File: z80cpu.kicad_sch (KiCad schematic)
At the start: 6 parts

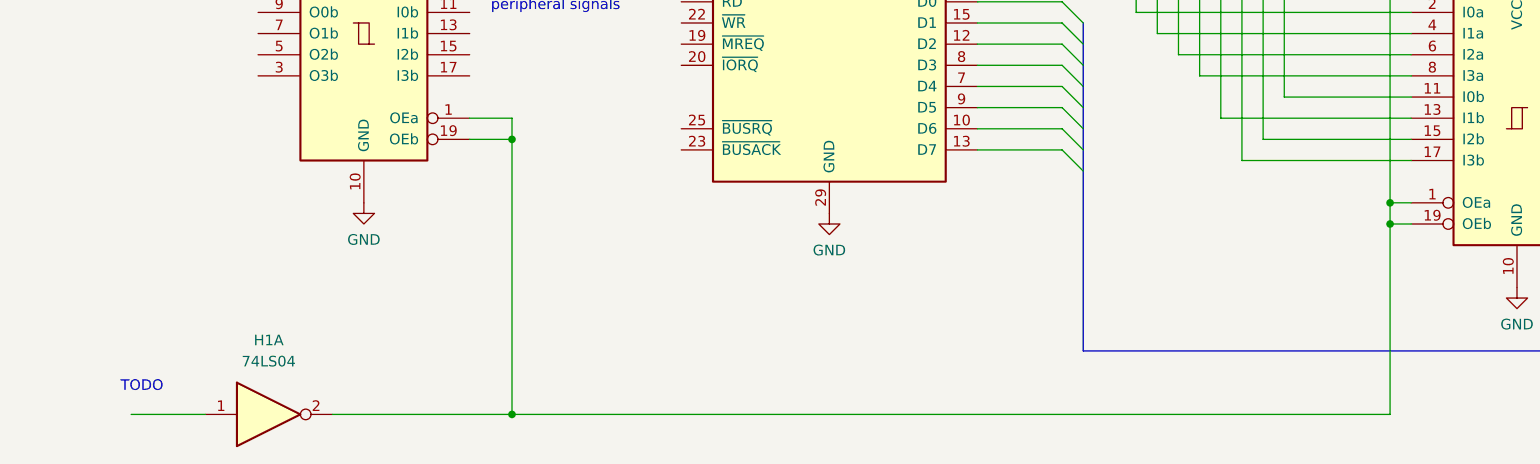
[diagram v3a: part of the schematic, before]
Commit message: Fixed addr order in mem mux, busack on z80 buffers
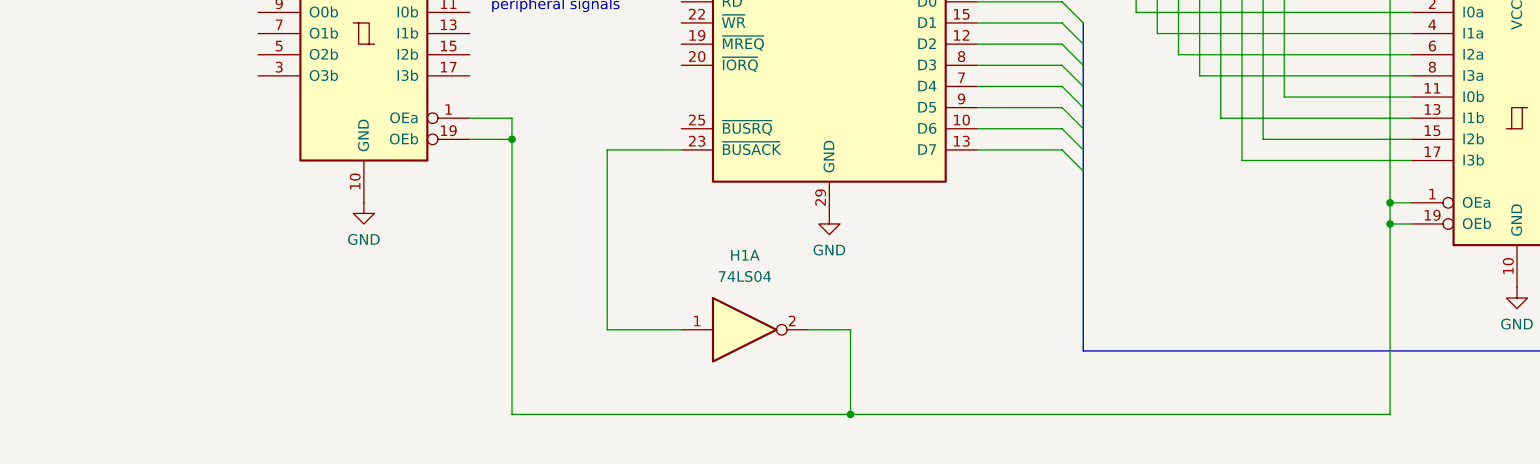
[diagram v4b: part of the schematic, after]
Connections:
- net at H1.1: now also F2-F5.23 (~{BUSACK})
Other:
- note removed: "TODO"
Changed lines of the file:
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@@
   (junction (at 182.88 54.61) (diameter 0) (color 0 0 0 0)
   )
+  (junction (at 118.11 134.62) (diameter 0) (color 0 0 0 0)
+  )
   (junction (at 182.88 111.76) (diameter 0) (color 0 0 0 0)
   )
   (junction (at 77.47 101.6) (diameter 0) (color 0 0 0 0)
   )
-  (junction (at 77.47 134.62) (diameter 0) (color 0 0 0 0)
-  )
   (junction (at 182.88 109.22) (diameter 0) (color 0 0 0 0)
   )
@@
     (stroke (width 0) (type default))
   )
-  (wire (pts (xy 31.75 134.62) (xy 40.64 134.62))
-    (stroke (width 0) (type default))
-  )
   (wire (pts (xy 170.18 46.99) (xy 170.18 57.15))
     (stroke (width 0) (type default))
@@
     (stroke (width 0) (type default))
   )
+  (wire (pts (xy 97.79 102.87) (xy 88.9 102.87))
+    (stroke (width 0) (type default))
+  )
   (wire (pts (xy 160.02 72.39) (xy 160.02 93.98))
     (stroke (width 0) (type default))
@@
     (stroke (width 0) (type default))
   )
+  (wire (pts (xy 88.9 102.87) (xy 88.9 124.46))
+    (stroke (width 0) (type default))
+  )
   (wire (pts (xy 133.35 85.09) (xy 143.51 85.09))
     (stroke (width 0) (type default))
@@
     (stroke (width 0) (type default))
   )
+  (wire (pts (xy 88.9 124.46) (xy 97.79 124.46))
+    (stroke (width 0) (type default))
+  )
   (wire (pts (xy 152.4 86.36) (xy 185.42 86.36))
     (stroke (width 0) (type default))
@@
     (stroke (width 0) (type default))
   )
+  (wire (pts (xy 118.11 134.62) (xy 182.88 134.62))
+    (stroke (width 0) (type default))
+  )
   (wire (pts (xy 133.35 52.07) (xy 165.1 52.07))
     (stroke (width 0) (type default))
@@
     (stroke (width 0) (type default))
   )
-  (wire (pts (xy 77.47 134.62) (xy 182.88 134.62))
+  (wire (pts (xy 77.47 134.62) (xy 118.11 134.62))
     (stroke (width 0) (type default))
   )
@@
     (stroke (width 0) (type default))
   )
+  (wire (pts (xy 118.11 124.46) (xy 118.11 134.62))
+    (stroke (width 0) (type default))
+  )
   (wire (pts (xy 133.35 95.25) (xy 143.51 95.25))
     (stroke (width 0) (type default))
@@
     (stroke (width 0) (type default))
   )
-  (wire (pts (xy 55.88 134.62) (xy 77.47 134.62))
-    (stroke (width 0) (type default))
-  )
   (wire (pts (xy 157.48 91.44) (xy 185.42 91.44))
     (stroke (width 0) (type default))
@@
     (stroke (width 0) (type default))
   )
+  (wire (pts (xy 113.03 124.46) (xy 118.11 124.46))
+    (stroke (width 0) (type default))
+  )
   (wire (pts (xy 210.82 41.91) (xy 220.98 41.91))
     (stroke (width 0) (type default))
@@
   (bus (pts (xy 223.52 101.6) (xy 223.52 104.14))
     (stroke (width 0) (type default))
-  )
-  (text "TODO" (at 30.48 132.08 0)
-    (effects (font (size 1.27 1.27)) (justify left bottom))
   )
   (text "TODO\n<-- Z80 to ---\nperipheral signals" (at 74.93 86.36 0)
@@
         (path "/12a6dbe3-008d-4c5b-88f6-9f1c816060be/1847fdc4-53d8-4940-8c5f-7a326599bae2"
           (reference "U?") (unit 1)
-        )
-      )
-    )
-  )
-  (symbol (lib_id "74xx:74LS04") (at 48.26 134.62 0) (unit 1)
-    (in_bom yes) (on_board yes) (dnp no) (fields_autoplaced)
-    (property "Reference" "H1" (at 48.26 125.73 0)
-      (effects (font (size 1.27 1.27)))
-    )
-    (property "Value" "74LS04" (at 48.26 128.27 0)
-      (effects (font (size 1.27 1.27)))
-    )
-    (property "Footprint" "" (at 48.26 134.62 0)
-      (effects (font (size 1.27 1.27)) hide)
-    )
-    (property "Datasheet" "http://www.ti.com/lit/gpn/sn74LS04" (at 48.26 134.62 0)
-      (effects (font (size 1.27 1.27)) hide)
-    )
-    (pin "1")
-    (pin "2")
-    (pin "3")
-    (pin "4")
-    (pin "5")
-    (pin "6")
-    (pin "8")
-    (pin "9")
-    (pin "10")
-    (pin "11")
-    (pin "12")
-    (pin "13")
-    (pin "14")
-    (pin "7")
-    (instances
-      (project "ceda"
-        (path "/12a6dbe3-008d-4c5b-88f6-9f1c816060be/1847fdc4-53d8-4940-8c5f-7a326599bae2"
-          (reference "H1") (unit 1)
         )
       )
@@
         )
       )
+    )
+  )
+  (symbol (lib_id "74xx:74LS04") (at 105.41 124.46 0) (unit 1)
+    (in_bom yes) (on_board yes) (dnp no) (fields_autoplaced)
+    (property "Reference" "H1" (at 105.41 115.57 0)
+      (effects (font (size 1.27 1.27)))
+    )
+    (property "Value" "74LS04" (at 105.41 118.11 0)
+      (effects (font (size 1.27 1.27)))
+    )
+    (property "Footprint" "" (at 105.41 124.46 0)
+      (effects (font (size 1.27 1.27)) hide)
+    )
+    (property "Datasheet" "http://www.ti.com/lit/gpn/sn74LS04" (at 105.41 124.46 0)
+      (effects (font (size 1.27 1.27)) hide)
+    )
+    (pin "1")
+    (pin "2")
+    (pin "3")
+    (pin "4")
+    (pin "5")
+    (pin "6")
+    (pin "8")
+    (pin "9")
+    (pin "10")
+    (pin "11")
+    (pin "12")
+    (pin "13")
+    (pin "14")
+    (pin "7")
+    (instances
+      (project "ceda"
+        (path "/12a6dbe3-008d-4c5b-88f6-9f1c816060be/1847fdc4-53d8-4940-8c5f-7a326599bae2"
+          (reference "H1") (unit 1)
+        )
+      )

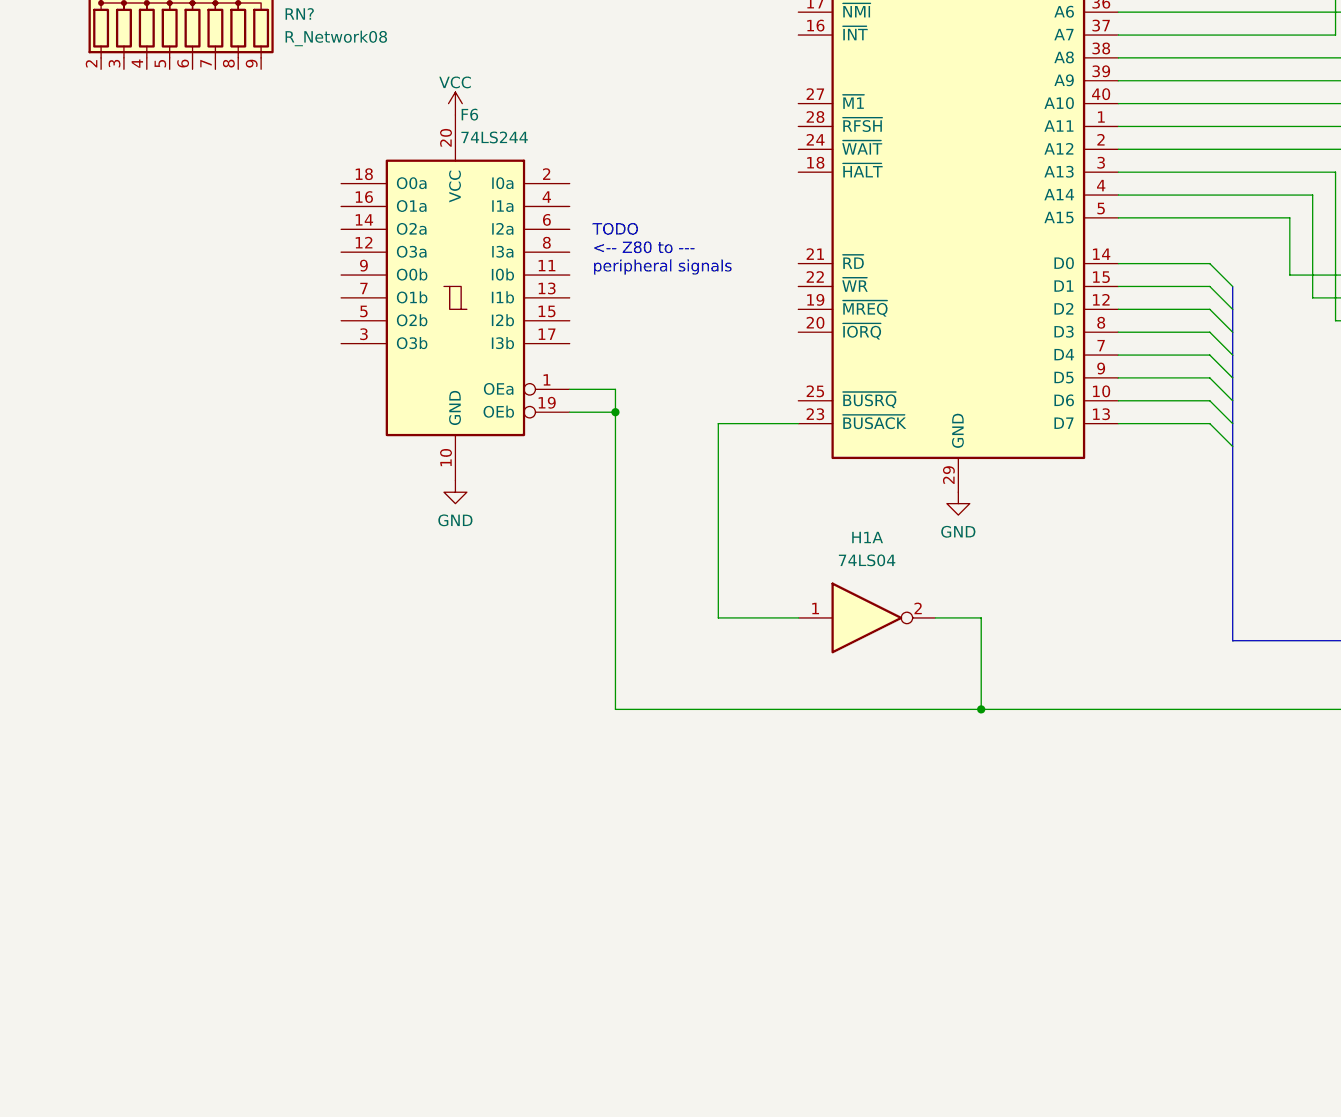
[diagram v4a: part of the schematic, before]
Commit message: Found both ROM CE and OE
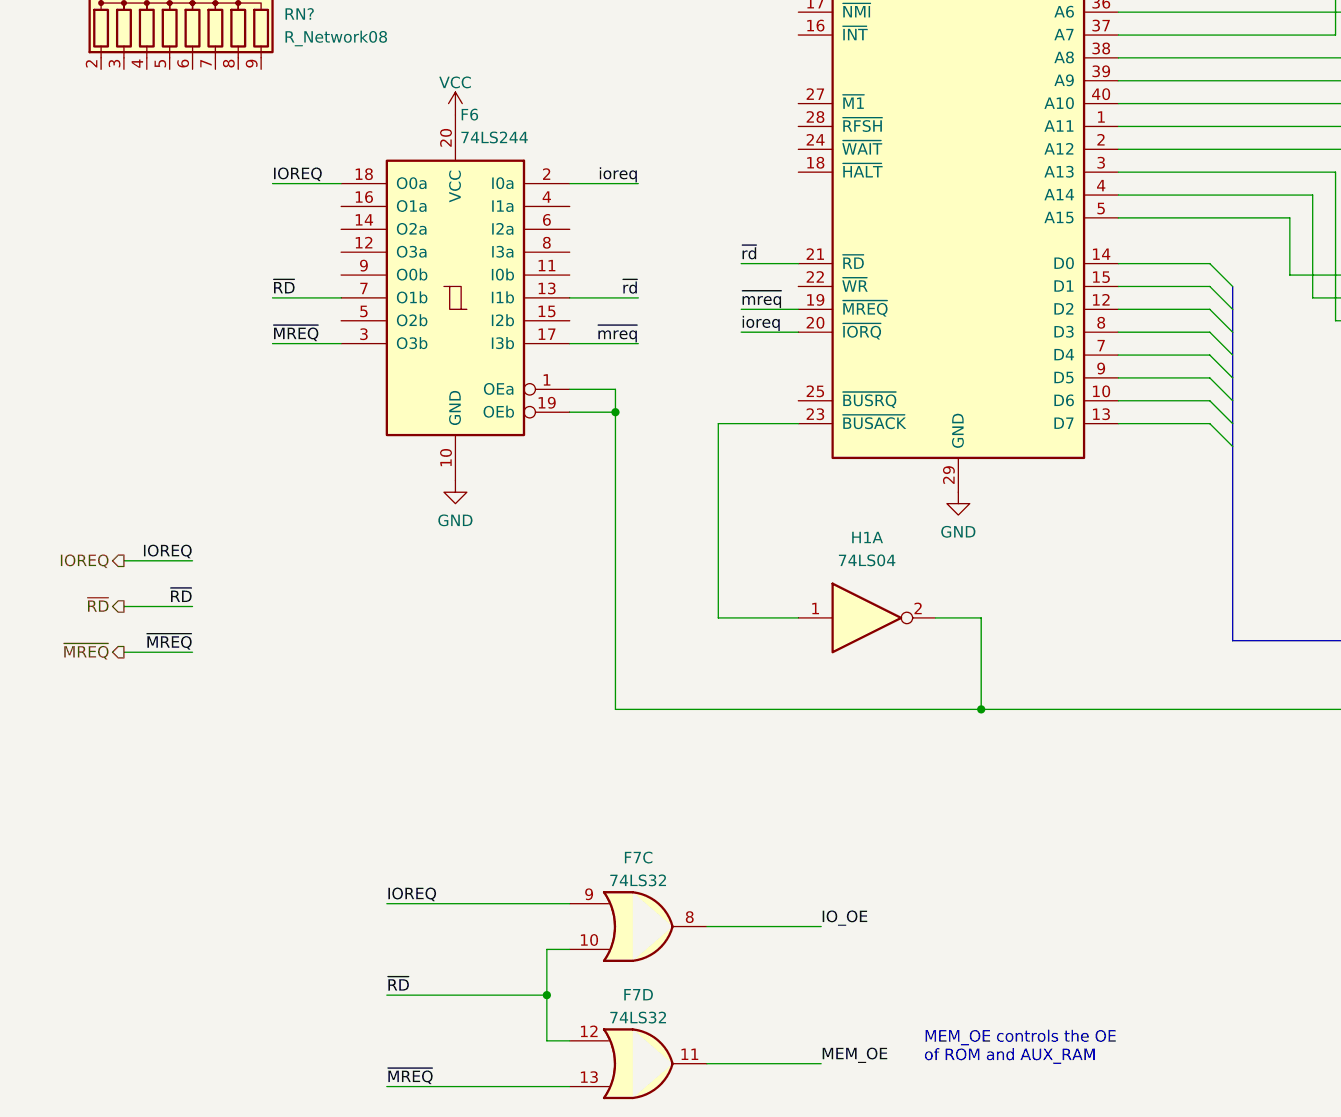
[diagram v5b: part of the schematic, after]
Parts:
- added F7: 74LS32, symbol 74xx:74LS32
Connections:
- net ~{mreq}: now reaches F2-F5.19 (~{MREQ})
- net ~{mreq}: now also F6.17 (I3b)
- net ioreq: now reaches F2-F5.20 (~{IORQ})
- net ioreq: now also F6.2 (I0a)
- net ~{rd}: now reaches F2-F5.21 (~{RD})
- net ~{rd}: now also F6.13 (I1b)
- net IOREQ: now reaches F6.18 (O0a)
- net IOREQ: now also F7.9
- net ~{MREQ}: now reaches F6.3 (O3b)
- net ~{MREQ}: now also F7.13
- net ~{RD}: now reaches F6.7 (O1b)
- net ~{RD}: now also F7.10, F7.12
- new net IO_OE: F7.8
- new net MEM_OE: F7.11
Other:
- note added: "MEM_OE controls the OE of ROM and AUX_RAM"
- note removed: "TODO <-- Z80 to --- peripheral signals"

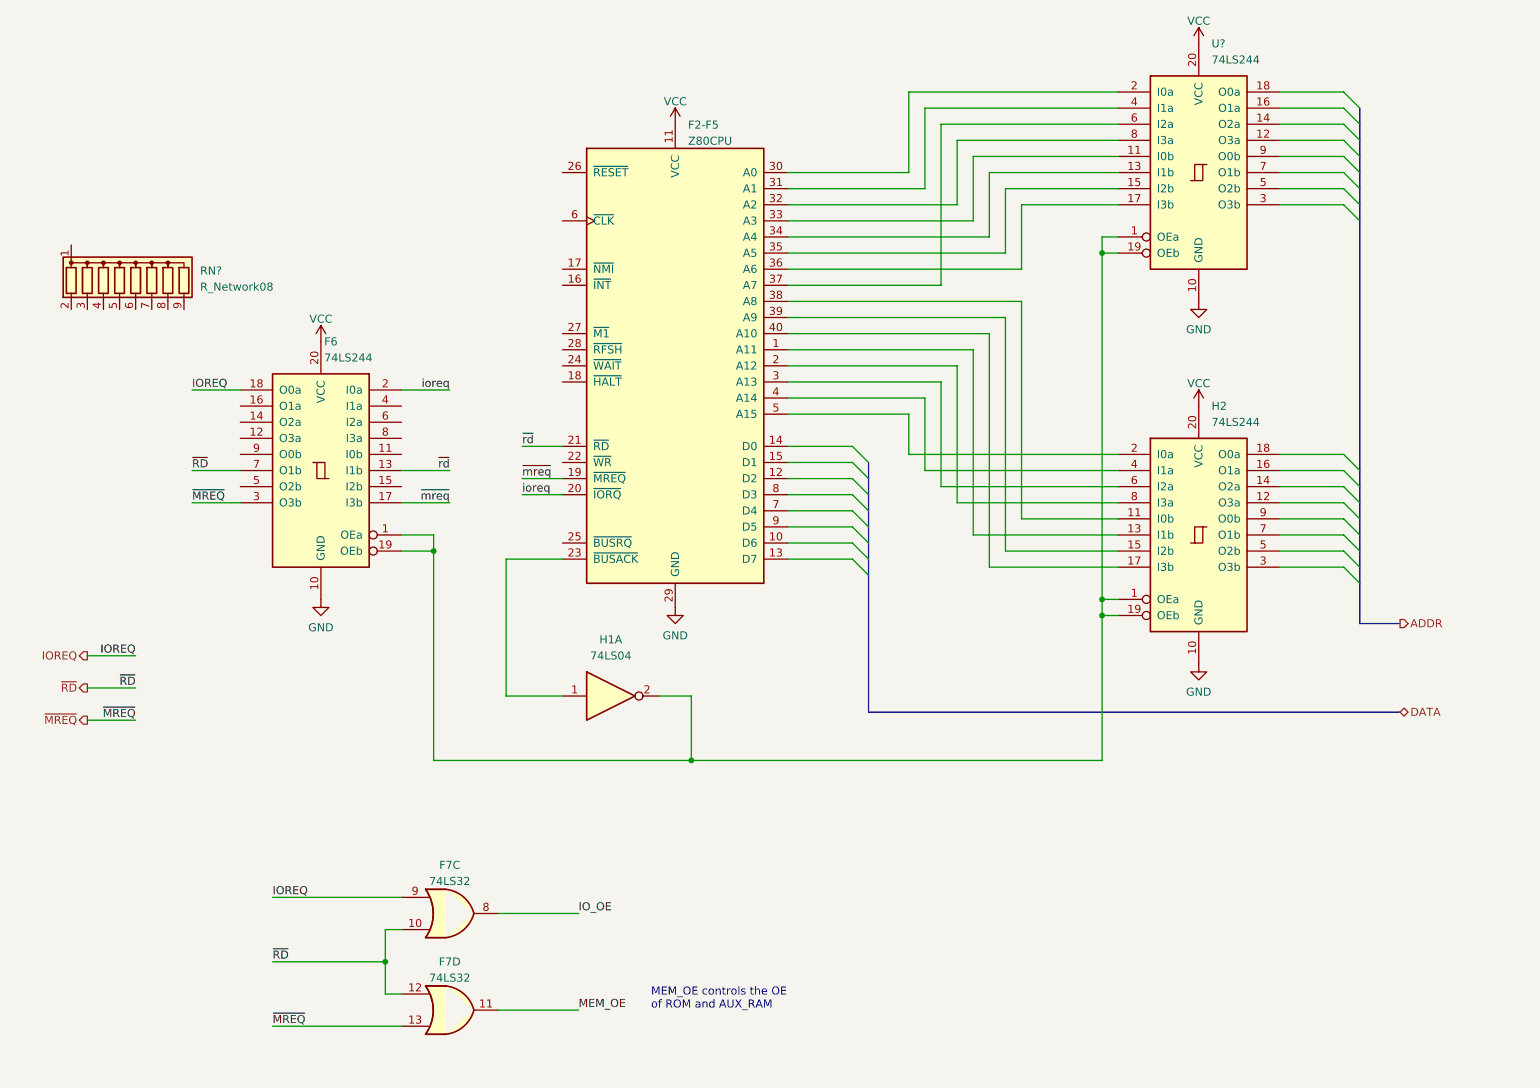
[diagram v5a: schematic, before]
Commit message: Found WR signal and fixed RD
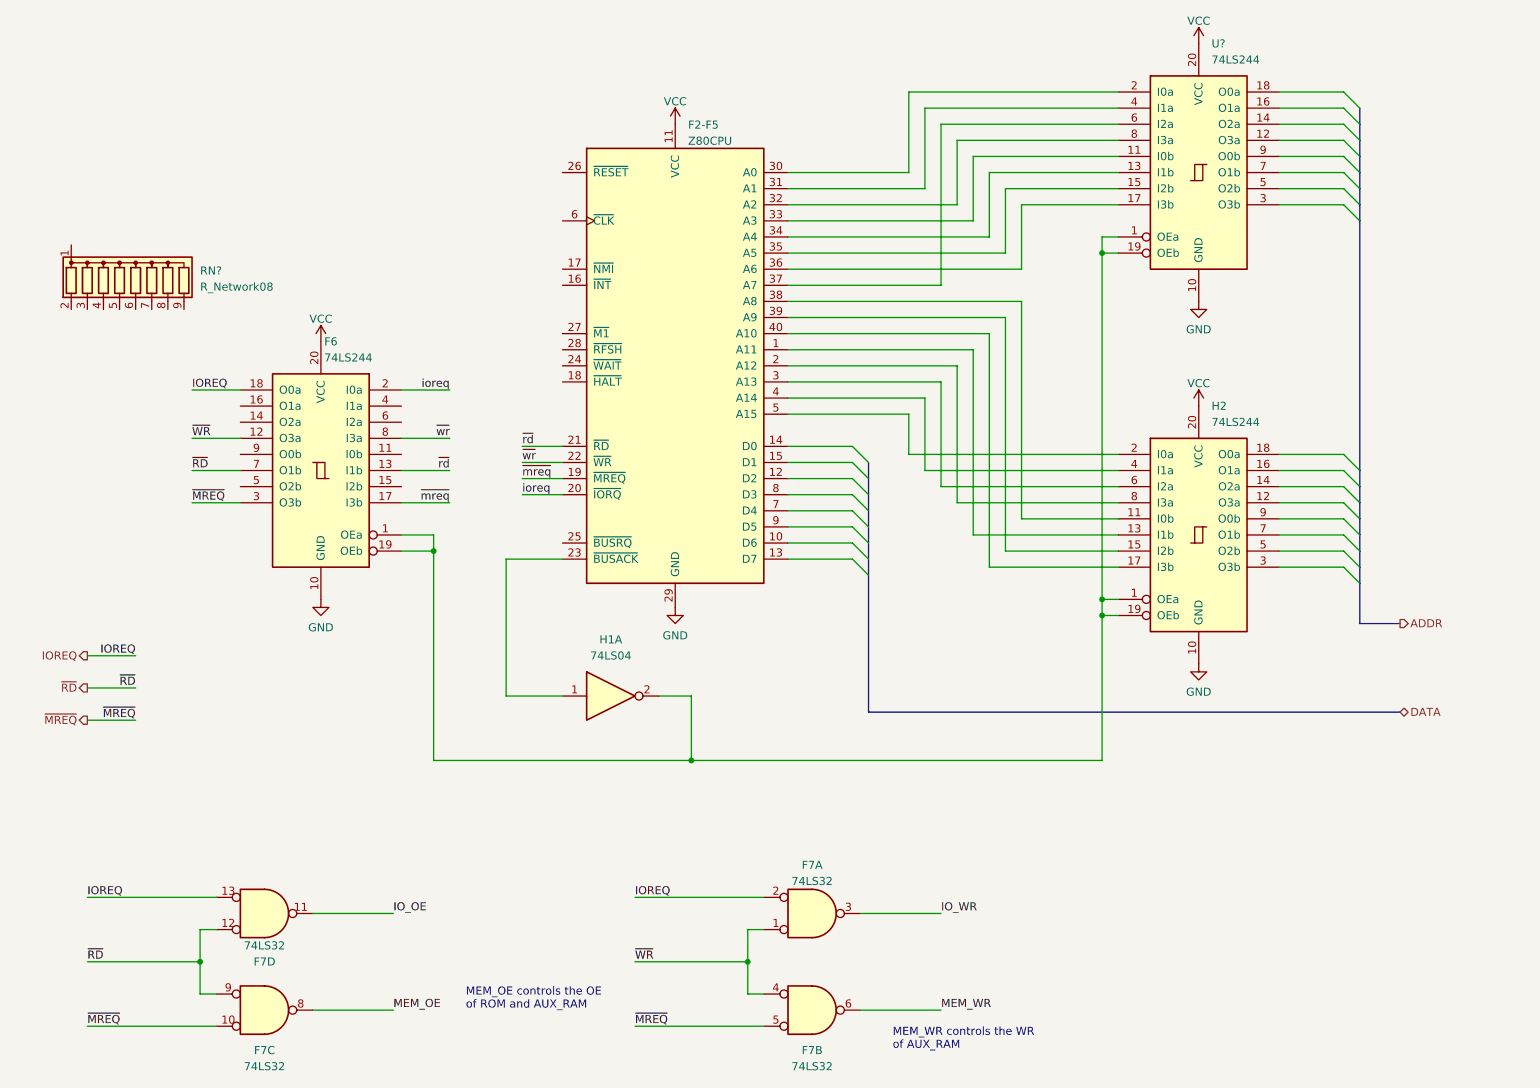
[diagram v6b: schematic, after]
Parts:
- added unit 2 of F7
- added unit 1 of F7
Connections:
- net IOREQ: now also F7.13, F7.2; no longer F7.9
- net IO_OE: now also F7.11; no longer F7.8
- net MEM_OE: now also F7.8; no longer F7.11
- net ~{MREQ}: now also F7.10, F7.5; no longer F7.13
- net ~{RD}: now also F7.9; no longer F7.10
- net ~{wr}: now reaches F2-F5.22 (~{WR})
- net ~{wr}: now also F6.8 (I3a)
- net ~{WR}: now reaches F6.12 (O3a)
- net ~{WR}: now also F7.1, F7.4
- new net IO_WR: F7.3
- new net MEM_WR: F7.6
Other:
- note added: "MEM_WR controls the WR of AUX_RAM"
